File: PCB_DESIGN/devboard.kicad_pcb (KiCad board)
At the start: 2 copper layers, 21 x 51 mm, 33 parts, among them J1 USB_C_Receptacle_USB2.0_14P, J2 Conn_01x20, J3 Conn_01x20, J4 Conn_01x03, SW1 SW_Push, U1 RP2040, U2 MCP1700x-330xxTT, U4 W25Q16JVUXIQ TR, Y1 12 MHz

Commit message: a bunch more routing
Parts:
- moved R2 55.3 mm to (162.5, 55.2)
- moved R1 51.8 mm to (159.5, 55.6), turned to -90 degrees
- moved R7 49.0 mm to (156.4, 66.6)
- moved C10 34.7 mm to (163.5, 81.9), turned to -90 degrees
- moved C11 30.8 mm to (163.4, 71.1)
- moved C7 28.4 mm to (162.7, 67.4)
- moved C6 26.6 mm to (161.7, 68.2)
- moved C12 17.5 mm to (160.7, 68.2)
- moved R3 0.33 mm to (161.3, 70.7)
- moved R4 0.33 mm to (162.4, 70.7)
- moved C8 0.18 mm to (165.7, 72.8)
- moved C1 0.17 mm to (165.8, 71.2)
- moved C5 0.17 mm to (164.3, 71.4)
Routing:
- net +3V3: track 0.00 -> 23.9 mm, vias 0 -> 2
- net XIN: track 0.00 -> 7.30 mm
- net +1V1: track 0.00 -> 6.01 mm
- net Net-(C16-Pad2): track 0.00 -> 3.46 mm
- net GND: track 0.00 -> 3.41 mm
- net Net-(J1-CC2): track 0.00 -> 2.08 mm
- net Net-(J1-CC1): track 0.00 -> 1.95 mm
- net XOUT: track 0.00 -> 1.82 mm
- net /USB_DP: track 17.7 -> 19.1 mm
- net /USB_DN: track 17.7 -> 19.1 mm
- net QSPI_SS: track 7.16 -> 8.44 mm

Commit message: more routing
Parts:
- moved R2 32.6 mm to (130.1, 51.6)
- moved R1 30.8 mm to (128.8, 53.9)
- moved C13 0.14 mm to (157.2, 55.4)
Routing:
- net /USB_DN: track 19.1 -> 22.0 mm
- net /USB_DP: track 19.1 -> 22.1 mm
- net Net-(J1-CC2): track 2.08 -> 0.00 mm
- net Net-(J1-CC1): track 1.95 -> 0.00 mm
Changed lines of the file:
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@@
 	(footprint "Capacitor_SMD:C_0603_1608Metric"
 		(layer "F.Cu")
-		(at 157.375 55.45 180)
+		(at 157.24 55.43 180)
 		(descr "Capacitor SMD 0603 (1608 Metric), square (rectangular) end terminal, IPC-7351 nominal, (Body size source: IPC-SM-782 page 76, https://www.pcb-3d.com/wordpress/wp-content/uploads/ipc-sm-782a_amendment_1_and_2.pdf), generated with kicad-footprint-generator")
 		(tags "capacitor")
@@
 	(footprint "Resistor_SMD:R_0402_1005Metric"
 		(layer "F.Cu")
-		(at 162.52 55.2)
+		(at 130.1 51.64)
 		(descr "Resistor SMD 0402 (1005 Metric), square (rectangular) end terminal, IPC-7351 nominal, (Body size source: IPC-SM-782 page 72, https://www.pcb-3d.com/wordpress/wp-content/uploads/ipc-sm-782a_amendment_1_and_2.pdf), generated with kicad-footprint-generator")
 		(tags "resistor")
@@
 	(footprint "Resistor_SMD:R_0402_1005Metric"
 		(layer "F.Cu")
-		(at 159.5 55.64 -90)
+		(at 128.79 53.93 -90)
 		(descr "Resistor SMD 0402 (1005 Metric), square (rectangular) end terminal, IPC-7351 nominal, (Body size source: IPC-SM-782 page 72, https://www.pcb-3d.com/wordpress/wp-content/uploads/ipc-sm-782a_amendment_1_and_2.pdf), generated with kicad-footprint-generator")
 		(tags "resistor")
@@
 	)
 	(segment
-		(start 161.9 53.295)
-		(end 161.9 55.09)
-		(width 0.2)
-		(layer "F.Cu")
-		(net 7)
-	)
-	(segment
-		(start 161.9 55.09)
-		(end 162.01 55.2)
-		(width 0.2)
-		(layer "F.Cu")
-		(net 7)
-	)
-	(segment
-		(start 158.9 53.295)
-		(end 158.9 54.53)
-		(width 0.2)
-		(layer "F.Cu")
-		(net 8)
-	)
-	(segment
-		(start 158.9 54.53)
-		(end 159.5 55.13)
-		(width 0.2)
-		(layer "F.Cu")
-		(net 8)
-	)
-	(segment
 		(start 161.65 71.575)
 		(end 161.325 71.25)
@@
 	)
 	(segment
-		(start 163.725 66.403198)
-		(end 163.725 67.83)
+		(start 160.851 54.321)
+		(end 160.9 54.272)
 		(width 0.2)
 		(layer "F.Cu")
@@
 	)
 	(segment
-		(start 163.725 67.83)
+		(start 159.949 54.321)
+		(end 160.851 54.321)
+		(width 0.2)
+		(layer "F.Cu")
+		(net 52)
+	)
+	(segment
+		(start 163.675 67.88)
 		(end 161.325 70.23)
 		(width 0.2)
@@
 	)
 	(segment
+		(start 159.9 54.272)
+		(end 159.949 54.321)
+		(width 0.2)
+		(layer "F.Cu")
+		(net 52)
+	)
+	(segment
 		(start 160.9 53.295)
 		(end 160.9 54.382501)
@@
 	)
 	(segment
+		(start 160.9 54.382501)
+		(end 160.925 54.407501)
+		(width 0.2)
+		(layer "F.Cu")
+		(net 52)
+	)
+	(segment
+		(start 160.9 54.272)
+		(end 160.9 53.295)
+		(width 0.2)
+		(layer "F.Cu")
+		(net 52)
+	)
+	(segment
 		(start 160.925 54.407501)
-		(end 160.925 63.603198)
+		(end 160.925 62.763198)
 		(width 0.2)
 		(layer "F.Cu")
@@
 	)
 	(segment
-		(start 160.925 63.603198)
-		(end 163.725 66.403198)
+		(start 160.925 62.763198)
+		(end 163.675 65.513198)
 		(width 0.2)
 		(layer "F.Cu")
@@
 	)
 	(segment
-		(start 160.9 54.382501)
-		(end 160.925 54.407501)
+		(start 159.9 53.295)
+		(end 159.9 54.272)
 		(width 0.2)
 		(layer "F.Cu")
@@
 	)
 	(segment
-		(start 164.175 68.016397)
-		(end 162.375 69.816397)
+		(start 163.675 65.513198)
+		(end 163.675 67.88)
+		(width 0.2)
+		(layer "F.Cu")
+		(net 52)
+	)
+	(segment
+		(start 161.4 53.295)
+		(end 161.4 54.382501)
 		(width 0.2)
 		(layer "F.Cu")
@@
 	)
 	(segment
-		(start 161.375 61.931705)
-		(end 161.375 63.416802)
+		(start 161.4 52.318)
+		(end 161.4 53.295)
 		(width 0.2)
 		(layer "F.Cu")
@@
 	)
 	(segment
-		(start 161.375 61.549449)
-		(end 161.375 61.931705)
+		(start 161.375 54.407501)
+		(end 161.375 57.456431)
 		(width 0.2)
 		(layer "F.Cu")
@@
 	)
 	(segment
-		(start 161.4 54.382501)
-		(end 161.375 54.407501)
+		(start 161.375 58.274203)
+		(end 161.375 58.656431)
 		(width 0.2)
 		(layer "F.Cu")
@@
 	)
 	(segment
-		(start 161.375 54.407501)
-		(end 161.375 60.731705)
+		(start 160.4 52.318)
+		(end 160.449 52.269)
 		(width 0.2)
 		(layer "F.Cu")
@@
 	)
 	(segment
-		(start 162.375 69.816397)
-		(end 162.375 70.23)
+		(start 161.592772 57.674203)
+		(end 161.592772 58.056431)
 		(width 0.2)
 		(layer "F.Cu")
@@
 	)
 	(segment
-		(start 161.592744 60.949449)
-		(end 161.592744 61.331705)
+		(start 164.125 65.326802)
+		(end 164.125 68.066397)
 		(width 0.2)
 		(layer "F.Cu")
@@
 	)
 	(segment
-		(start 161.375 63.416802)
-		(end 161.78568 63.827482)
+		(start 161.351 52.269)
+		(end 161.4 52.318)
 		(width 0.2)
 		(layer "F.Cu")
@@
 	)
 	(segment
-		(start 161.78568 63.827482)
-		(end 164.175 66.216802)
+		(start 160.4 53.295)
+		(end 160.4 52.318)
 		(width 0.2)
 		(layer "F.Cu")
@@
 	)
 	(segment
-		(start 161.4 53.295)
-		(end 161.4 54.382501)
+		(start 161.375 62.576802)
+		(end 164.125 65.326802)
+		(width 0.2)
+		(layer "F.Cu")
+		(net 53)
+	)
+	(segment
+		(start 164.125 68.066397)
+		(end 162.375 69.816397)
+		(width 0.2)
+		(layer "F.Cu")
+		(net 53)
+	)
+	(segment
+		(start 161.4 54.382501)
+		(end 161.375 54.407501)
+		(width 0.2)
+		(layer "F.Cu")
+		(net 53)
+	)
+	(segment
+		(start 162.375 69.816397)
+		(end 162.375 70.23)
+		(width 0.2)
+		(layer "F.Cu")
+		(net 53)
+	)
+	(segment
+		(start 161.375 59.006899)
+		(end 161.375 62.576802)
+		(width 0.2)
+		(layer "F.Cu")
+		(net 53)
+	)
+	(segment
+		(start 160.449 52.269)
+		(end 161.351 52.269)
 		(width 0.2)
 		(layer "F.Cu")
@@
 	)
 	(segment
-		(start 164.175 66.216802)
-		(end 164.175 68.016397)
+		(start 161.375 58.656431)
+		(end 161.375 59.006899)
 		(width 0.2)
 		(layer "F.Cu")
@@
 	)
 	(arc
-		(start 161.483872 60.840577)
-		(mid 161.560856 60.872465)
-		(end 161.592744 60.949449)
+		(start 161.592772 58.056431)
+		(mid 161.56088 58.133425)
+		(end 161.483886 58.165317)
 		(width 0.2)
 		(layer "F.Cu")
@@
 	)
 	(arc
-		(start 161.483872 61.440577)
-		(mid 161.406888 61.472465)
-		(end 161.375 61.549449)
+		(start 161.375 57.456431)
+		(mid 161.406892 57.533425)
+		(end 161.483886 57.565317)
 		(width 0.2)
 		(layer "F.Cu")
@@
 	)
 	(arc
-		(start 161.375 60.731705)
-		(mid 161.406888 60.808689)
-		(end 161.483872 60.840577)
+		(start 161.483886 57.565317)
+		(mid 161.56088 57.597209)
+		(end 161.592772 57.674203)
 		(width 0.2)
 		(layer "F.Cu")
@@
 	)
 	(arc
-		(start 161.592744 61.331705)
-		(mid 161.560856 61.408689)
-		(end 161.483872 61.440577)
+		(start 161.483886 58.165317)
+		(mid 161.406892 58.197209)
+		(end 161.375 58.274203)
 		(width 0.2)
 		(layer "F.Cu")
@@
 		(base_line
 			(pts
-				(xy 161.375 60.731705) (xy 161.375 63.416802) (xy 161.78568 63.827482)
+				(xy 161.375 57.456431) (xy 161.375 59.006899)
 			)
 		)
 		(base_line_coupled
 			(pts
-				(xy 160.925 60.731705) (xy 160.925 60.724923)
+				(xy 160.925 57.456431) (xy 160.925 57.485045)
 			)
 		)
 		(corner_radius_percent 80)
 		(end
-			(xy 161.78568 63.827482)
+			(xy 161.375 59.006899)
 		)
 		(initial_side "left")
@@
 		(last_status "tuned")
 		(last_track_width 0.2)
-		(last_tuning "-0.0000 mm (tuned)")
+		(last_tuning "0.0000 mm (tuned)")
 		(max_amplitude 1)
 		(min_amplitude 0.2)
 		(min_spacing 0.6)
 		(origin
-			(xy 161.375 60.731705)
+			(xy 161.375 57.456431)
 		)
 		(override_custom_rules no)
@@
 		(target_skew_min -0.1)
 		(tuning_mode "diff_pair_skew")
-		(members "388217bf-80fe-4966-91ab-1fef31f0705a" "44e215db-f893-4cb5-9f9a-4ad43e6947a3"
-			"6c336c21-84e7-4b23-bd76-9f1d2dc7652d" "9685e99c-eaf2-4d59-a04d-15197acb6df6"
-			"af7bce77-1e13-4ce3-a51a-2e46e108f95d" "af87f04b-4198-4d65-8b6d-4fc78ba90811"
-			"ccfe41c6-b32b-44c6-8287-e8cada238d56" "d6b9d577-4578-449f-97ea-e0f18fd91c6a"
+		(members "119ba522-a0e5-4296-b156-d5c8eae1ab2f" "5c59161c-0046-4faa-bda6-c0ae4bce4979"
+			"612de78e-7b02-4cd3-ad93-68a53e4ec73b" "78337e57-4f32-4bad-ad61-5728684c1f07"
+			"a11753a0-ff85-4dc2-a399-36682c0366e9" "e00c0e2f-7576-4940-b4c5-d7848bdac26a"
+			"fe963958-9da1-4888-9b0b-7eb75645fe76"
 		)
 	)

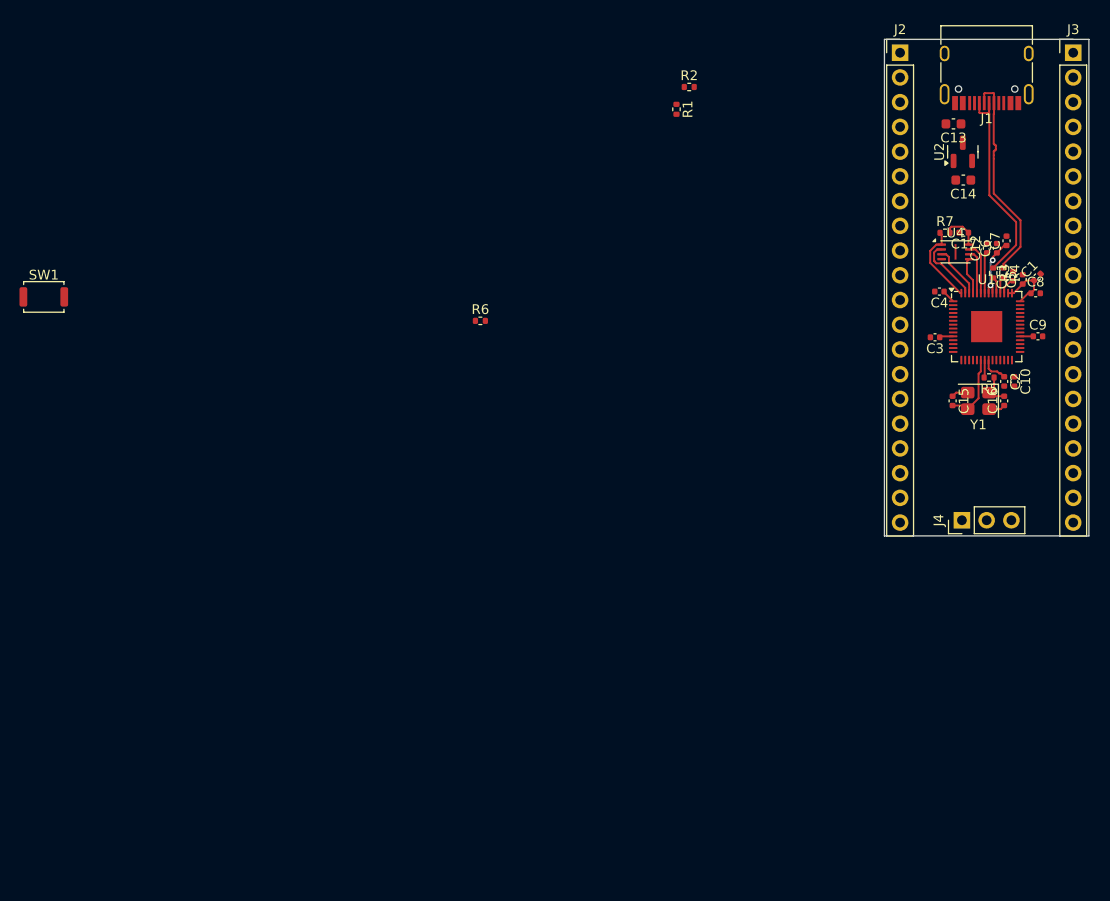
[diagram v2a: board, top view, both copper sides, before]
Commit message: finished routing signals
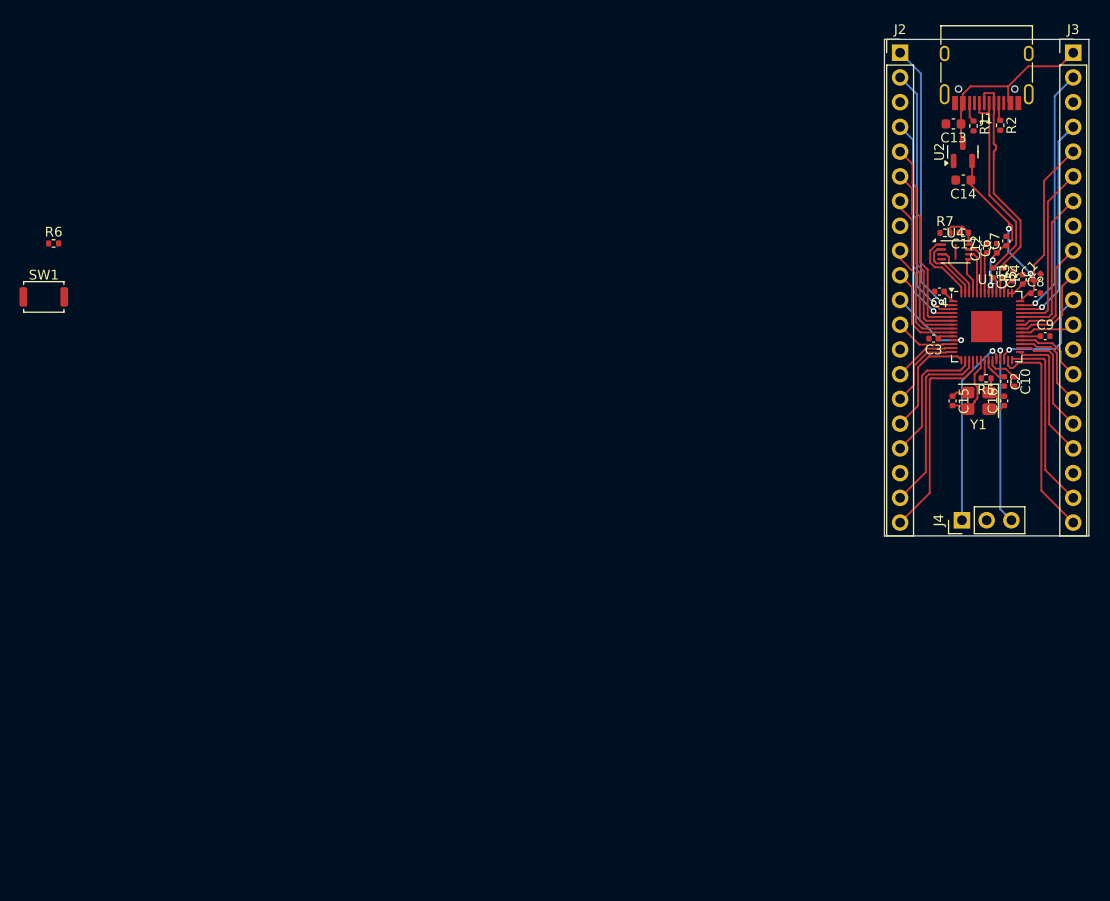
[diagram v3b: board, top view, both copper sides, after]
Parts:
- moved R6 44.5 mm to (64.8, 67.7)
- moved R2 32.2 mm to (162.0, 55.6), turned to -90 degrees
- moved R1 30.6 mm to (159.3, 55.6)
- moved C9 0.75 mm to (166.7, 77.2)
- moved R5 0.32 mm to (160.6, 81.6)
- moved C3 0.20 mm to (155.2, 77.5)
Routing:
- net +3V3: track 23.9 -> 57.1 mm, vias 2 -> 4
- net GPIO0: track 0.00 -> 28.7 mm, vias 0 -> 1
- net GPIO1: track 0.00 -> 26.9 mm, vias 0 -> 1
- net GPIO29_ADC3: track 0.00 -> 26.4 mm, vias 0 -> 1
- net GPIO2: track 0.00 -> 22.4 mm, vias 0 -> 1
- net GPIO28_ADC2: track 0.00 -> 22.2 mm, vias 0 -> 1
- net GPIO16: track 0.00 -> 22.0 mm
- net GPIO15: track 0.00 -> 21.8 mm
- net GPIO3: track 0.00 -> 20.7 mm
- net VBUS: track 0.00 -> 20.1 mm
- net SWCLK: track 0.00 -> 19.8 mm, vias 0 -> 1
- net GPIO14: track 0.00 -> 19.1 mm
- net SWD: track 0.00 -> 18.9 mm, vias 0 -> 1
- net GPIO17: track 0.00 -> 18.9 mm
- net GPIO4: track 0.00 -> 18.7 mm
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
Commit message: some ground fill stuff
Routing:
- net QSPI_SD2: track 5.43 -> 8.64 mm
- net GND: track 3.41 -> 4.89 mm, vias 0 -> 12
- net QSPI_SS: track 7.54 -> 8.81 mm
- net +3V3: track 57.1 -> 57.9 mm
- added copper zone on B.Cu, net GND
- added copper zone on F.Cu, net GND
